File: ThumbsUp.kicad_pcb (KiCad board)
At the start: 2 copper layers, 400 x 336.1 mm, 169 parts, among them IC1 RP2040, IC2 W25Q128JVSIM, J1 Conn_01x04_Male, J10 Raiser_Male, J11 Raiser_Female, J12 Raiser_Male, J13 Raiser_Female, J14 Raiser_Male, J15 Raiser_Female, J16 Raiser_Male, J17 Raiser_Female, J18 Raiser_Male, J19 52559-1233, J2 Conn_01x04_Male, J20 Conn_01x04_Female, J21 Conn_01x04_Female, J22 Conn_01x04_Female, J23 Conn_01x04_Female, J24 Conn_01x04_Male, J25 Conn_01x04_Male, J26 Conn_01x04_Male, J27 Conn_01x04_Male, J28 Conn_01x04_Female, J29 Conn_01x04_Female, J3 Conn_01x04_Female, J30 Conn_01x04_Female, J31 Conn_01x04_Female, J32 USB_C_Receptacle_USB2.0, J4 Conn_01x04_Male, J5 Conn_01x04_Female, J6 Conn_01x04_Male, J7 Conn_01x04_Male, J8 Conn_01x04_Male, J9 Raiser_Female, U1 NCP1117-3.3_SOT223, Y1 ABLS-12.000MHZ-B4-T

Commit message: Traced bottom PCB.
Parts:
- D45, D46: moved to B.Cu
- moved D45 27.0 mm to (108.8, 212.8), turned to 270 degrees
- moved D46 25.5 mm to (106.3, 212.8), turned to 270 degrees
- moved RUN1 21.0 mm to (123.0, 224.5)
- moved BOOTSEL1 7.99 mm to (133.2, 224.5)
- moved D5 3.40 mm to (124.4, 200.4)
- moved D7 3.40 mm to (129.1, 200.4)
- moved D8 3.40 mm to (131.5, 200.4)
- moved D16 3.40 mm to (122.0, 200.4)
- moved D6 3.40 mm to (126.8, 200.4)
- moved D21 3.40 mm to (133.9, 200.4)
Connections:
- BOOTSEL1 pad A1: GND -> Net-(BOOTSEL1-PadA1)
- BOOTSEL1 pad C1: GND -> Net-(BOOTSEL1-PadA1)
- IC1 pad 11: Net-(IC1-Pad11) -> (no net)
- IC1 pad 12: Net-(IC1-Pad12) -> (no net)
- IC1 pad 13: Net-(IC1-Pad13) -> (no net)
- IC1 pad 14: Net-(IC1-Pad14) -> (no net)
- IC1 pad 15: Net-(IC1-Pad15) -> (no net)
- IC1 pad 16: Net-(IC1-Pad16) -> (no net)
- IC1 pad 17: Net-(IC1-Pad17) -> (no net)
- IC1 pad 18: Net-(IC1-Pad18) -> (no net)
- IC1 pad 24: Net-(IC1-Pad24) -> (no net)
- IC1 pad 25: Net-(IC1-Pad25) -> (no net)
- IC1 pad 26: GND -> Net-(IC1-Pad26)
- IC1 pad 27: Net-(IC1-Pad27) -> (no net)
- IC1 pad 28: Net-(IC1-Pad28) -> (no net)
- IC1 pad 31: Net-(IC1-Pad31) -> (no net)
- IC1 pad 32: Net-(IC1-Pad32) -> (no net)
- J10 pad 1: Net-(J10-Pad1) -> (no net)
- J10 pad 2: Net-(J10-Pad2) -> (no net)
- J10 pad 3: Net-(J10-Pad3) -> (no net)
- J10 pad 4: Net-(J10-Pad4) -> (no net)
- J32 pad A8: Net-(J32-PadA8) -> (no net)
- J32 pad B8: Net-(J32-PadB8) -> (no net)
- R3 pad 1: GND -> Net-(BOOTSEL1-PadA1)
- RUN1 pad A1: GND -> Net-(IC1-Pad26)
- RUN1 pad C1: GND -> Net-(IC1-Pad26)
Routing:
- net GND: track 360.4 -> 210.4 mm, vias 21 -> 16
- net COLA: track 83.7 -> 173.2 mm
- net Net-(J1-Pad1): track 0.00 -> 86.2 mm
- net Net-(J29-Pad1): track 0.00 -> 80.6 mm, vias 0 -> 1
- net Net-(J7-Pad1): track 0.00 -> 79.9 mm, vias 0 -> 1
- net Net-(J1-Pad4): track 0.00 -> 79.8 mm
- net Net-(J2-Pad1): track 0.00 -> 79.8 mm, vias 0 -> 1
- net Net-(J8-Pad1): track 0.00 -> 79.7 mm, vias 0 -> 1
- net Net-(J30-Pad1): track 0.00 -> 78.5 mm, vias 0 -> 1
- net COL1: track 50.5 -> 126.9 mm
- net Net-(J1-Pad3): track 0.00 -> 75.7 mm
- net Net-(J28-Pad1): track 0.00 -> 75.5 mm
- net Net-(J31-Pad1): track 0.00 -> 74.4 mm, vias 0 -> 1
- net Net-(J28-Pad4): track 0.00 -> 73.0 mm
- net COL3: track 51.6 -> 124.4 mm, vias 1 -> 2
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- removed copper zone on F.Cu, net GND

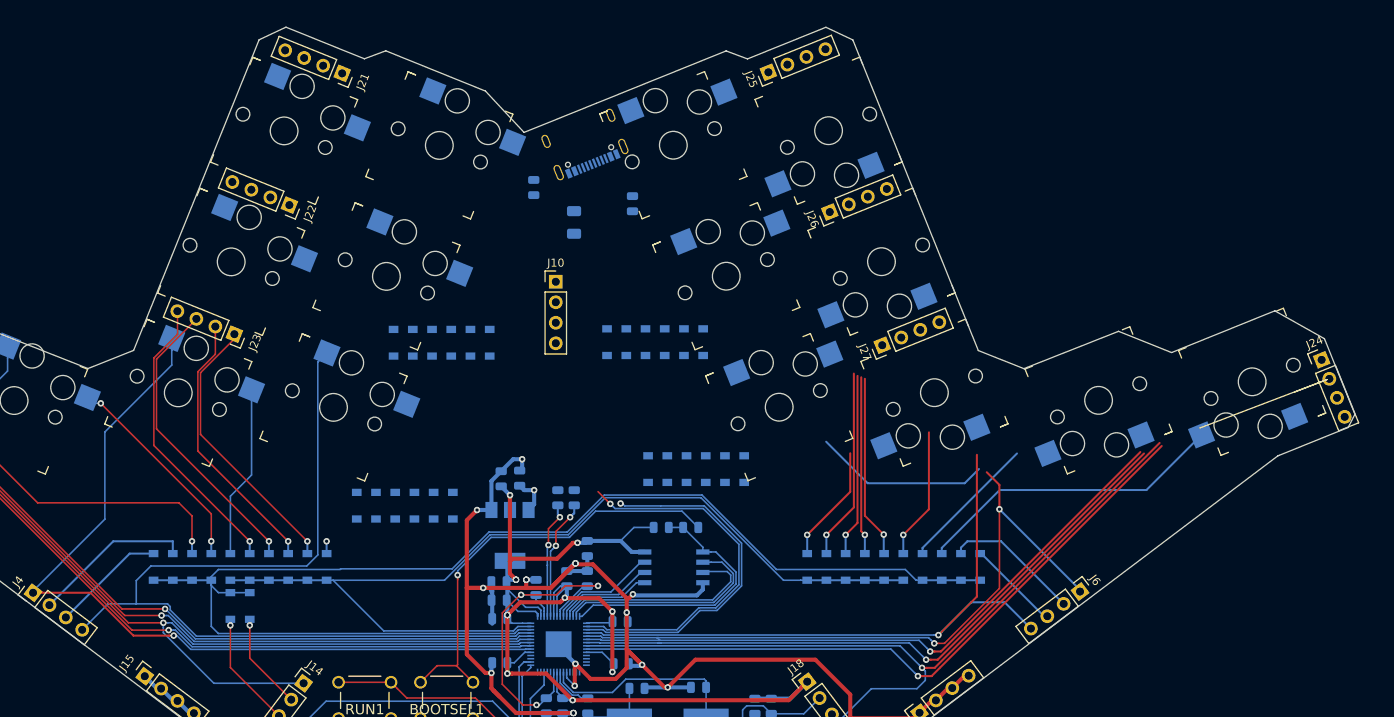
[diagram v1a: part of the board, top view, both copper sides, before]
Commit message: Traced middle PCB.
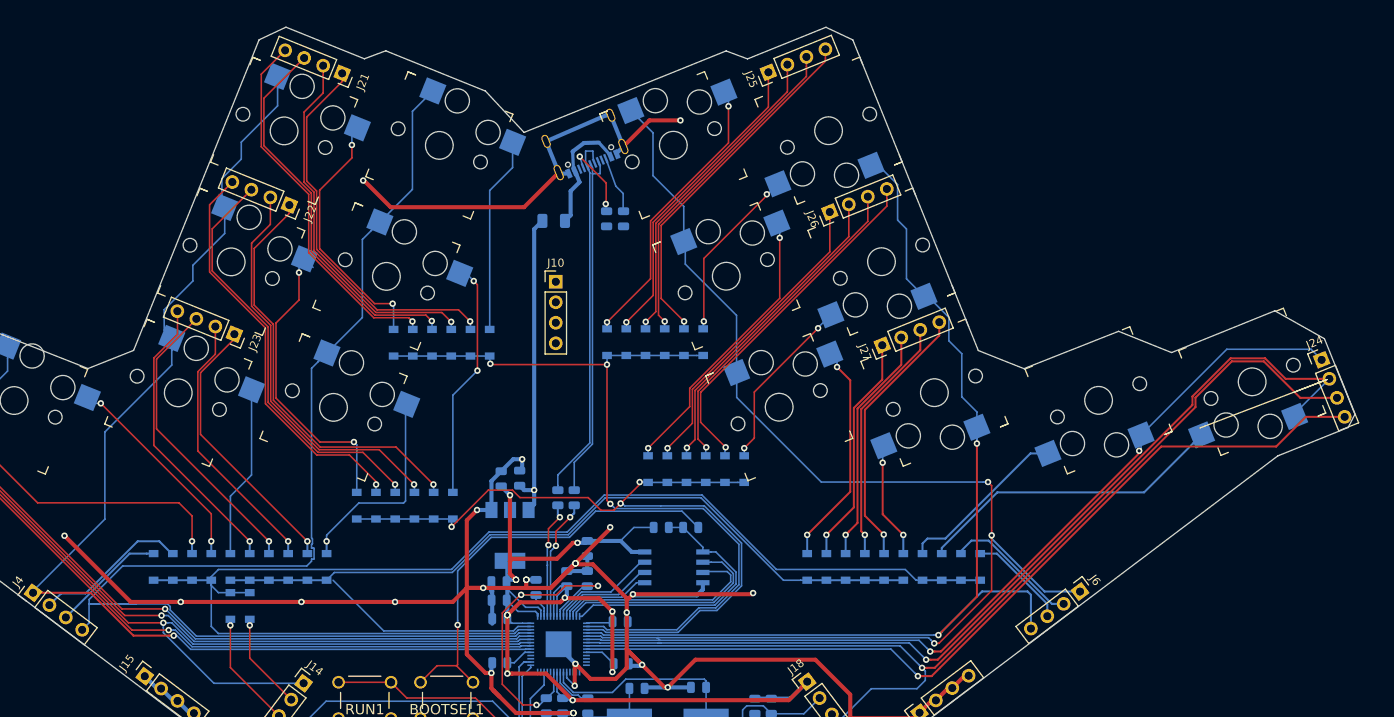
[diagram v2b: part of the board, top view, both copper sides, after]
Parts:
- moved R8 9.82 mm to (152.9, 164.8), turned to 270 degrees
- moved F1 2.53 mm to (146.4, 165.1), turned to 0 degrees
- moved R9 2.17 mm to (155.1, 164.8), turned to 90 degrees
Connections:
- J10 pad 1: (no net) -> GND
- J10 pad 2: (no net) -> GND
- J10 pad 3: (no net) -> GND
- J10 pad 4: (no net) -> GND
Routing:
- net GND: track 210.4 -> 341.0 mm, vias 16 -> 24
- net ROW0: track 46.5 -> 102.2 mm, vias 1 -> 3
- net ROW1: track 44.1 -> 97.8 mm, vias 1 -> 3
- net Net-(D6-Pad2): track 0.00 -> 52.1 mm, vias 0 -> 1
- net Net-(D8-Pad2): track 0.00 -> 52.1 mm, vias 0 -> 1
- net COL6: track 105.8 -> 157.7 mm, vias 2 -> 3
- net Net-(D5-Pad2): track 0.00 -> 50.5 mm, vias 0 -> 1
- net COL5: track 111.2 -> 161.4 mm
- net Net-(D7-Pad2): track 0.00 -> 50.2 mm, vias 0 -> 1
- net Net-(D2-Pad2): track 0.00 -> 48.0 mm, vias 0 -> 1
- net Net-(D4-Pad2): track 0.00 -> 47.9 mm, vias 0 -> 1
- net Net-(D1-Pad2): track 0.00 -> 46.1 mm, vias 0 -> 1
- net Net-(D3-Pad2): track 0.00 -> 46.0 mm, vias 0 -> 1
- net D-: track 0.00 -> 45.8 mm
- net COL7: track 82.5 -> 128.3 mm, vias 1 -> 2
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
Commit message: Traced top PCB, tweaked tracks here and there.
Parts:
- turned MX30 to 217 degrees
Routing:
- net Net-(J13-Pad3): track 0.00 -> 76.3 mm
- net Net-(J13-Pad4): track 0.00 -> 63.9 mm
- net Net-(J5-Pad2): track 80.5 -> 40.9 mm, vias 1 -> 2
- net SCL-TOP: track 13.9 -> 36.5 mm
- net Net-(J5-Pad4): track 38.6 -> 16.1 mm
- net Net-(J13-Pad2): track 0.00 -> 18.1 mm
- net SDA-TOP: track 20.3 -> 33.6 mm
- net Net-(J3-Pad3): track 71.7 -> 59.1 mm
- net Net-(J5-Pad3): track 26.9 -> 14.4 mm
- net VCC-TOP: track 18.0 -> 26.8 mm
- net Net-(J5-Pad1): track 91.8 -> 84.3 mm
- net Net-(J3-Pad2): track 43.2 -> 35.9 mm
- net Net-(J13-Pad1): track 0.00 -> 5.65 mm
- net Net-(J3-Pad1): track 35.4 -> 32.7 mm
- net GND-TOP: track 41.7 -> 44.4 mm
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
